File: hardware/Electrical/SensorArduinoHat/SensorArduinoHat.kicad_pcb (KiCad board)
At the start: 2 copper layers, 68.6 x 53.3 mm, 8 parts, among them J1 Power, J2 Digital/PWM, J3 Analog, J4 Digital/PWM

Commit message: updated readme, and fixed library linking for the arduino hat board
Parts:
- added C1: 10uF, Capacitor_THT:C_Rect_L4.0mm_W2.5mm_P2.50mm, F.Cu at (222.0, 76.7)
- added C2: 10uF, Capacitor_THT:C_Rect_L4.0mm_W2.5mm_P2.50mm, F.Cu at (222.0, 80.7)
- added C3: 10uF, Capacitor_THT:C_Rect_L4.0mm_W2.5mm_P2.50mm, F.Cu at (222.0, 84.8)
- added D1: 1N4001, Diode_THT:D_DO-41_SOD81_P10.16mm_Horizontal, F.Cu at (208.3, 76.8)
- added D2: 1N4001, Diode_THT:D_DO-41_SOD81_P10.16mm_Horizontal, F.Cu at (208.3, 81.0)
- added D3: 1N4001, Diode_THT:D_DO-41_SOD81_P10.16mm_Horizontal, F.Cu at (208.3, 85.3)
- added JBtn1: Conn_01x02, Connector_JST:JST_PH_B2B-PH-K_1x02_P2.00mm_Vertical, F.Cu at (181.5, 49.5)
- added JBtn2: Conn_01x02, Connector_JST:JST_PH_B2B-PH-K_1x02_P2.00mm_Vertical, F.Cu at (181.5, 56.0)
- added JBtn3: Conn_01x02, Connector_JST:JST_PH_B2B-PH-K_1x02_P2.00mm_Vertical, F.Cu at (181.5, 62.6)
- added JPIRL1: Conn_01x03, Connector_JST:JST_PH_B3B-PH-K_1x03_P2.00mm_Vertical, F.Cu at (221.2, 49.5)
- added JPIRR1: Conn_01x03, Connector_JST:JST_PH_B3B-PH-K_1x03_P2.00mm_Vertical, F.Cu at (221.2, 56.0)
- added JPwr1: Conn_01x02, Connector_JST:JST_PH_B2B-PH-K_1x02_P2.00mm_Vertical, F.Cu at (181.5, 69.1)
- added JRFID1: Conn_01x08, Connector_JST:JST_PH_B8B-PH-K_1x08_P2.00mm_Vertical, F.Cu at (197.5, 70.8)
- added JRFID_SWITCH1: Conn_01x02, Connector_JST:JST_PH_B2B-PH-K_1x02_P2.00mm_Vertical, F.Cu at (181.5, 75.7)
- added JUltrasonicL1: Conn_01x04, Connector_JST:JST_PH_B4B-PH-K_1x04_P2.00mm_Vertical, F.Cu at (197.5, 77.4)
- added JUltrasonicM1: Conn_01x04, Connector_JST:JST_PH_B4B-PH-K_1x04_P2.00mm_Vertical, F.Cu at (197.5, 83.9)
- added JUltrasonicR1: Conn_01x04, Connector_JST:JST_PH_B4B-PH-K_1x04_P2.00mm_Vertical, F.Cu at (197.5, 90.5)
- added R1: 10k, Resistor_THT:R_Axial_DIN0204_L3.6mm_D1.6mm_P5.08mm_Horizontal, F.Cu at (188.0, 69.7)
- added R2: 10k, Resistor_THT:R_Axial_DIN0204_L3.6mm_D1.6mm_P5.08mm_Horizontal, F.Cu at (188.0, 72.8)
- added R3: 10k, Resistor_THT:R_Axial_DIN0204_L3.6mm_D1.6mm_P5.08mm_Horizontal, F.Cu at (188.0, 76.0)
- added R4: 10k, Resistor_THT:R_Axial_DIN0204_L3.6mm_D1.6mm_P5.08mm_Horizontal, F.Cu at (188.0, 79.1)
- added R5: 10k, Resistor_THT:R_Axial_DIN0204_L3.6mm_D1.6mm_P5.08mm_Horizontal, F.Cu at (188.0, 82.3)
- added R6: 10k, Resistor_THT:R_Axial_DIN0204_L3.6mm_D1.6mm_P5.08mm_Horizontal, F.Cu at (188.0, 85.4)
- added R7: 10k, Resistor_THT:R_Axial_DIN0204_L3.6mm_D1.6mm_P5.08mm_Horizontal, F.Cu at (188.0, 88.6)
- added R8: 10k, Resistor_THT:R_Axial_DIN0204_L3.6mm_D1.6mm_P5.08mm_Horizontal, F.Cu at (188.0, 91.7)
- added U1: CD74HC14E, CD74HC14E:N14, F.Cu at (195.6, 65.0)
- added U2: CD4050BE, CD4050BE:N16, F.Cu at (206.2, 66.3)
- added U3: SN74AHC86N, CD74HC14E:N14, F.Cu at (216.7, 65.0)
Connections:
- net /SCL/A5 renamed /RFID Card Trigger
- net /SDA/A4 renamed /BtnPin3
- J1 pad 5: +5V -> 5V

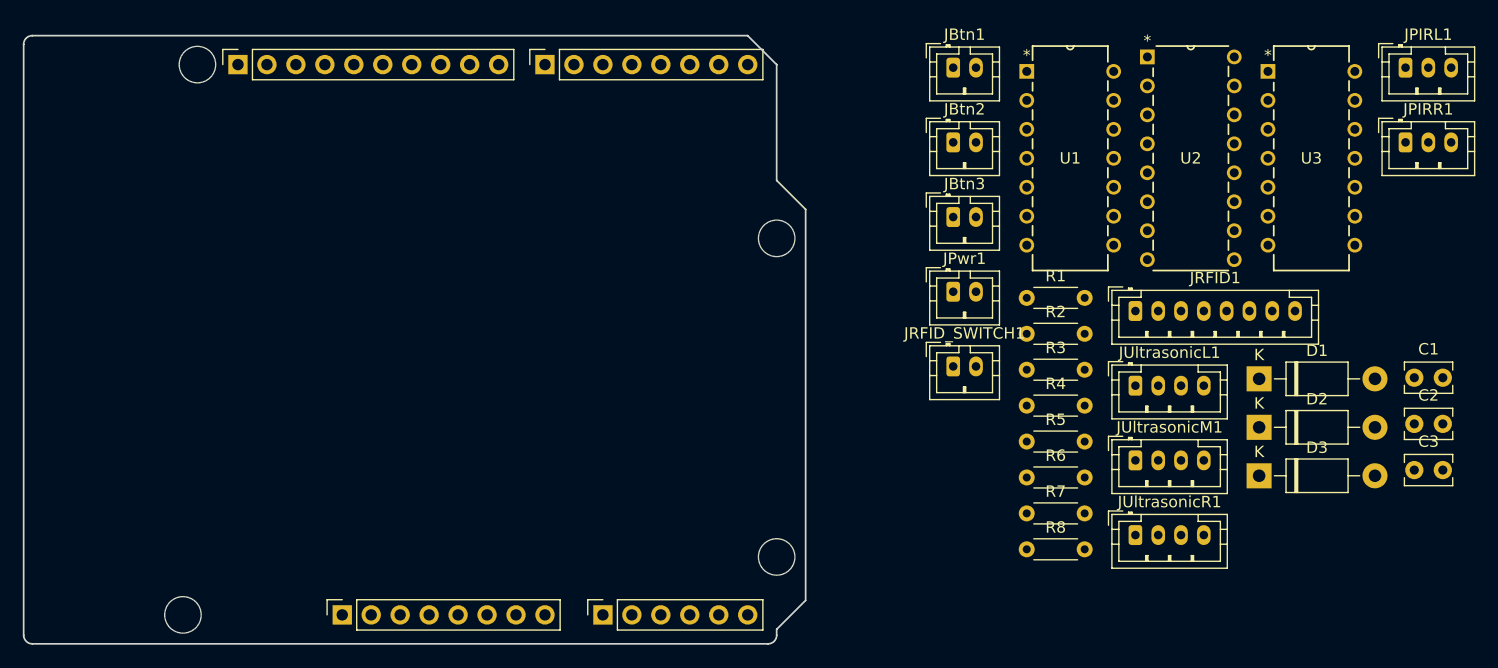
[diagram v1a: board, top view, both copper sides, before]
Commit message: layout complete for sensor box arduino hat
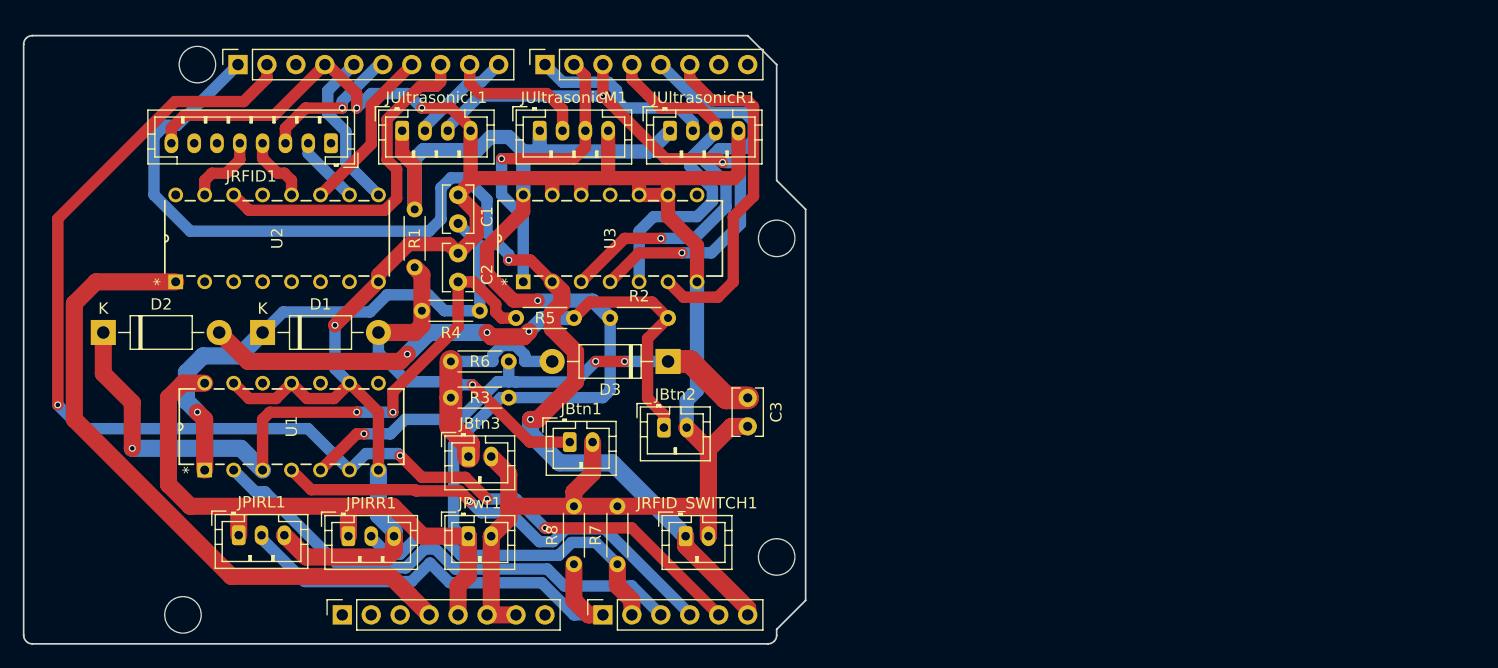
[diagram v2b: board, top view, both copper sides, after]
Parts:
- moved JPIRL1 110.2 mm to (118.9, 90.5)
- moved D2 101.7 mm to (107.0, 72.7)
- moved JPIRR1 98.9 mm to (128.5, 90.6)
- moved D1 87.5 mm to (121.0, 72.7)
- moved C1 84.9 mm to (138.1, 63.1), turned to 90 degrees
- moved C2 84.8 mm to (138.1, 68.2), turned to 90 degrees
- moved U2 75.3 mm to (131.1, 60.6), turned to 90 degrees
- moved JRFID1 72.1 mm to (127.0, 56.1), turned to 180 degrees
- moved JUltrasonicL1 68.1 mm to (133.2, 55.0)
- moved U1 65.6 mm to (131.1, 77.1), turned to 90 degrees
- moved JUltrasonicM1 59.7 mm to (145.3, 55.0)
- moved C3 58.8 mm to (163.5, 78.4), turned to -90 degrees
- moved U3 57.9 mm to (159.1, 60.6), turned to 90 degrees
- moved R1 54.2 mm to (134.3, 61.9), turned to -90 degrees
- moved JUltrasonicR1 54.1 mm to (156.7, 55.0)
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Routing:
- net GND: track 0.00 -> 228.2 mm, vias 0 -> 3
- net 5V: track 0.00 -> 145.6 mm, vias 0 -> 1
- net /BtnPin3: track 0.00 -> 107.8 mm, vias 0 -> 4
- net /RFID Card Trigger: track 0.00 -> 104.0 mm, vias 0 -> 2
- net Net-(D2-K): track 0.00 -> 60.2 mm, vias 0 -> 3
- net +3V3: track 0.00 -> 58.1 mm
- net Net-(D2-A): track 0.00 -> 54.4 mm, vias 0 -> 3
- net /*5: track 0.00 -> 50.8 mm, vias 0 -> 3
- net Net-(D1-K): track 0.00 -> 46.8 mm, vias 0 -> 1
- net Net-(D3-K): track 0.00 -> 44.5 mm, vias 0 -> 3
- net /A2: track 0.00 -> 44.1 mm
- net /A3: track 0.00 -> 41.2 mm, vias 0 -> 1
- net /A0: track 0.00 -> 40.6 mm
- net /*3: track 0.00 -> 36.9 mm, vias 0 -> 1
- net Net-(D1-A): track 0.00 -> 31.2 mm, vias 0 -> 1
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
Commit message: tweaked to include part values on silkscreen
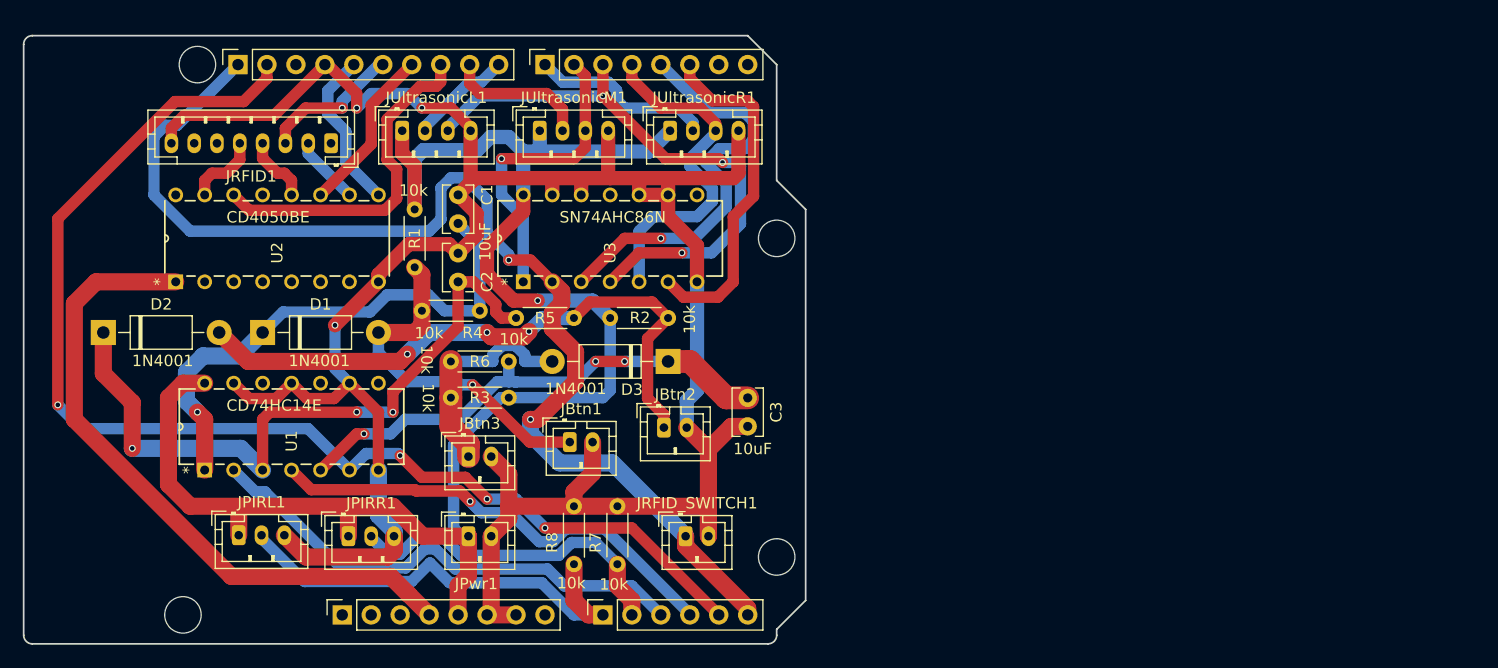
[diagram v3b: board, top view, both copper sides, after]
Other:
- board text added: "10k"
- board text added: "10uF"
- board text added: "1N4001"
- board text added: "CD4050BE"
- board text added: "CD74HC14E"
- board text added: "SN74AHC86N"
